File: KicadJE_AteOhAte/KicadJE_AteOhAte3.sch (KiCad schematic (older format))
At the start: 60 parts, among them U301 TL072, U302 TL072

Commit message: RIAA Basic Circuit
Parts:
- removed C301, C302, C303, C304: 10n, Capacitor_SMD:C_0805_2012Metric_Pad1.15x1.40mm_HandSolder, symbol Device:C
- removed D301, D302, D304, D305, D306, D307: LL4148, Diode_SMD:D_MiniMELF, symbol Diode:LL4148
- removed J? (x2): Conn_Coaxial_x2, symbol Connector:Conn_Coaxial_x2
- removed R301, R304, R306, R311, R316, R319, R322, R324: 1k, Resistor_SMD:R_0805_2012Metric_Pad1.15x1.40mm_HandSolder, symbol Device:R
- removed R303, R308, R314, R317, R318, R327, R329: 10k, Resistor_SMD:R_0805_2012Metric_Pad1.15x1.40mm_HandSolder, symbol Device:R
- removed R309, R323: 10R, Resistor_SMD:R_0805_2012Metric_Pad1.15x1.40mm_HandSolder, symbol Device:R
- removed R313, R315: 100k, Resistor_SMD:R_0805_2012Metric_Pad1.15x1.40mm_HandSolder, symbol Device:R
- removed R320, R321: Open, Resistor_SMD:R_0805_2012Metric_Pad1.15x1.40mm_HandSolder, symbol Device:R
- removed R325, R326: 0R, Resistor_SMD:R_0805_2012Metric_Pad1.15x1.40mm_HandSolder, symbol Device:R
- removed R328, R330: OPEN, Resistor_SMD:R_0805_2012Metric_Pad1.15x1.40mm_HandSolder, symbol Device:R
- added C305, C306, C315, C316: 10u, Capacitor_THT:CP_Radial_D6.3mm_P2.50mm, symbol Device:CP
- added C? (x4): 47p, symbol Device:C_Small
- added C? (x2): 100u, Capacitor_THT:CP_Radial_D6.3mm_P2.50mm, symbol Device:CP
- added C? (x4): 470n, symbol Device:C_Small
- added C? (x6): 470n_THT, Capacitor_THT:C_Rect_L7.2mm_W5.5mm_P5.00mm_FKS2_FKP2_MKS2_MKP2, symbol Device:C_Small
- added C? (x2): 470n, Capacitor_SMD:C_1206_3216Metric_Pad1.42x1.75mm_HandSolder, symbol Device:C_Small
- added C? (x2): 1n_THT, Capacitor_THT:C_Rect_L7.2mm_W5.5mm_P5.00mm_FKS2_FKP2_MKS2_MKP2, symbol Device:C_Small
- added C? (x2): 1n, Capacitor_SMD:C_1206_3216Metric_Pad1.42x1.75mm_HandSolder, symbol Device:C_Small
- added C? (x2): 680p_THT, Capacitor_THT:C_Rect_L7.2mm_W5.5mm_P5.00mm_FKS2_FKP2_MKS2_MKP2, symbol Device:C_Small
- added C? (x2): 680p, Capacitor_SMD:C_1206_3216Metric_Pad1.42x1.75mm_HandSolder, symbol Device:C_Small
- added C? (x2): 2n2_THT, Capacitor_THT:C_Rect_L7.2mm_W5.5mm_P5.00mm_FKS2_FKP2_MKS2_MKP2, symbol Device:C_Small
- added C? (x2): 2n2, Capacitor_SMD:C_1206_3216Metric_Pad1.42x1.75mm_HandSolder, symbol Device:C_Small
- added C? (x2): 100n, Capacitor_SMD:C_0805_2012Metric_Pad1.15x1.40mm_HandSolder, symbol Device:C
- added J301: PJRAS2X2S01AUX, PJRAS2X2S01AUX, symbol PJRAS2X2S01AUX:PJRAS2X2S01AUX
- added R? (x2): 680k, Resistor_SMD:R_0805_2012Metric_Pad1.15x1.40mm_HandSolder, symbol Device:R
- added R? (x5): 470R, Resistor_SMD:R_0805_2012Metric_Pad1.15x1.40mm_HandSolder, symbol Device:R
- added R? (x2): 47k, Resistor_SMD:R_0805_2012Metric_Pad1.15x1.40mm_HandSolder, symbol Device:R
- added R? (x5): 2k2, Resistor_SMD:R_0805_2012Metric_Pad1.15x1.40mm_HandSolder, symbol Device:R
- added R?: 220R, Resistor_SMD:R_0805_2012Metric_Pad1.15x1.40mm_HandSolder, symbol Device:R
- added R? (x4): 18k, Resistor_SMD:R_0805_2012Metric_Pad1.15x1.40mm_HandSolder, symbol Device:R
- added R? (x2): 1M, Resistor_SMD:R_0805_2012Metric_Pad1.15x1.40mm_HandSolder, symbol Device:R
- added R? (x2): 82k, Resistor_SMD:R_0805_2012Metric_Pad1.15x1.40mm_HandSolder, symbol Device:R
- added U? (x3): TL072, AJ-Dropbox-Kicad:AJ_SO-8_5.3x6.2mm_P1.27mm, symbol Amplifier_Operational:TL072
- C307: renamed from C306; value 1u -> 10u
- C313: renamed from C310; value 1u -> 10u
- R302: value 10k -> 220R
- R304: renamed from R305; value 1k -> 2k2
- R305: renamed from R307; value 10k -> 470R
- R311: renamed from R310; value 1k -> 12k
- R312: value 10k -> 18k
- gave numbers to parts that had none: 2
- renumbered C308 to C309, C309 to C310
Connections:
- net labels added: L_GainOut, L_Rumble_Out, R_GainOut, R_Rumble_Out
- net labels removed: Out1_Dist, Out1_Final, Out2_Dist, Out2_Final
- wire segments 145 -> 242
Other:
- moved on the sheet: C307, C308, C313, C314, D303, D308, D309, D310, R302, R304, R305, R311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

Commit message: SCH Annotate
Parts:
- gave numbers to parts that had none: 57
- renumbered C305 to C331, C306 to C332, C307 to C333, C308 to C334, C309 to C336, C310 to C337, C311 to C339, C312 to C340, C313 to C341, C314 to C342, C315 to C343, C316 to C344, D308 to D301, D309 to D302, D310 to D303, D303 to D304, R302 to R301, R304 to R302, R305 to R307, R311 to R327, U301 to U302, U302 to U303

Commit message: RIAA RCA
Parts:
- J301: footprint PJRAS2X2S01AUX -> AJ:PJRAS2X2S01AUX_RCA
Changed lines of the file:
@@
 F 0 "J301" H 6475 6850 50  0001 L BNN
 F 1 "PJRAS2X2S01AUX" H 6475 6850 50  0001 L BNN
-F 2 "PJRAS2X2S01AUX" H 6475 6850 50  0001 L BNN
+F 2 "AJ:PJRAS2X2S01AUX_RCA" H 6475 6850 50  0001 L BNN
 F 3 "" H 6475 6850 50  0001 L BNN
 F 4 "PJRAS2X2S01AUX" H 6475 6850 50  0001 L BNN "Field4"
@@
 F 0 "J301" H 4425 6850 50  0001 L BNN
 F 1 "PJRAS2X2S01AUX" H 4425 6850 50  0001 L BNN
-F 2 "PJRAS2X2S01AUX" H 4425 6850 50  0001 L BNN
+F 2 "AJ:PJRAS2X2S01AUX_RCA" H 4425 6850 50  0001 L BNN
 F 3 "" H 4425 6850 50  0001 L BNN
 F 4 "PJRAS2X2S01AUX" H 4425 6850 50  0001 L BNN "Field4"

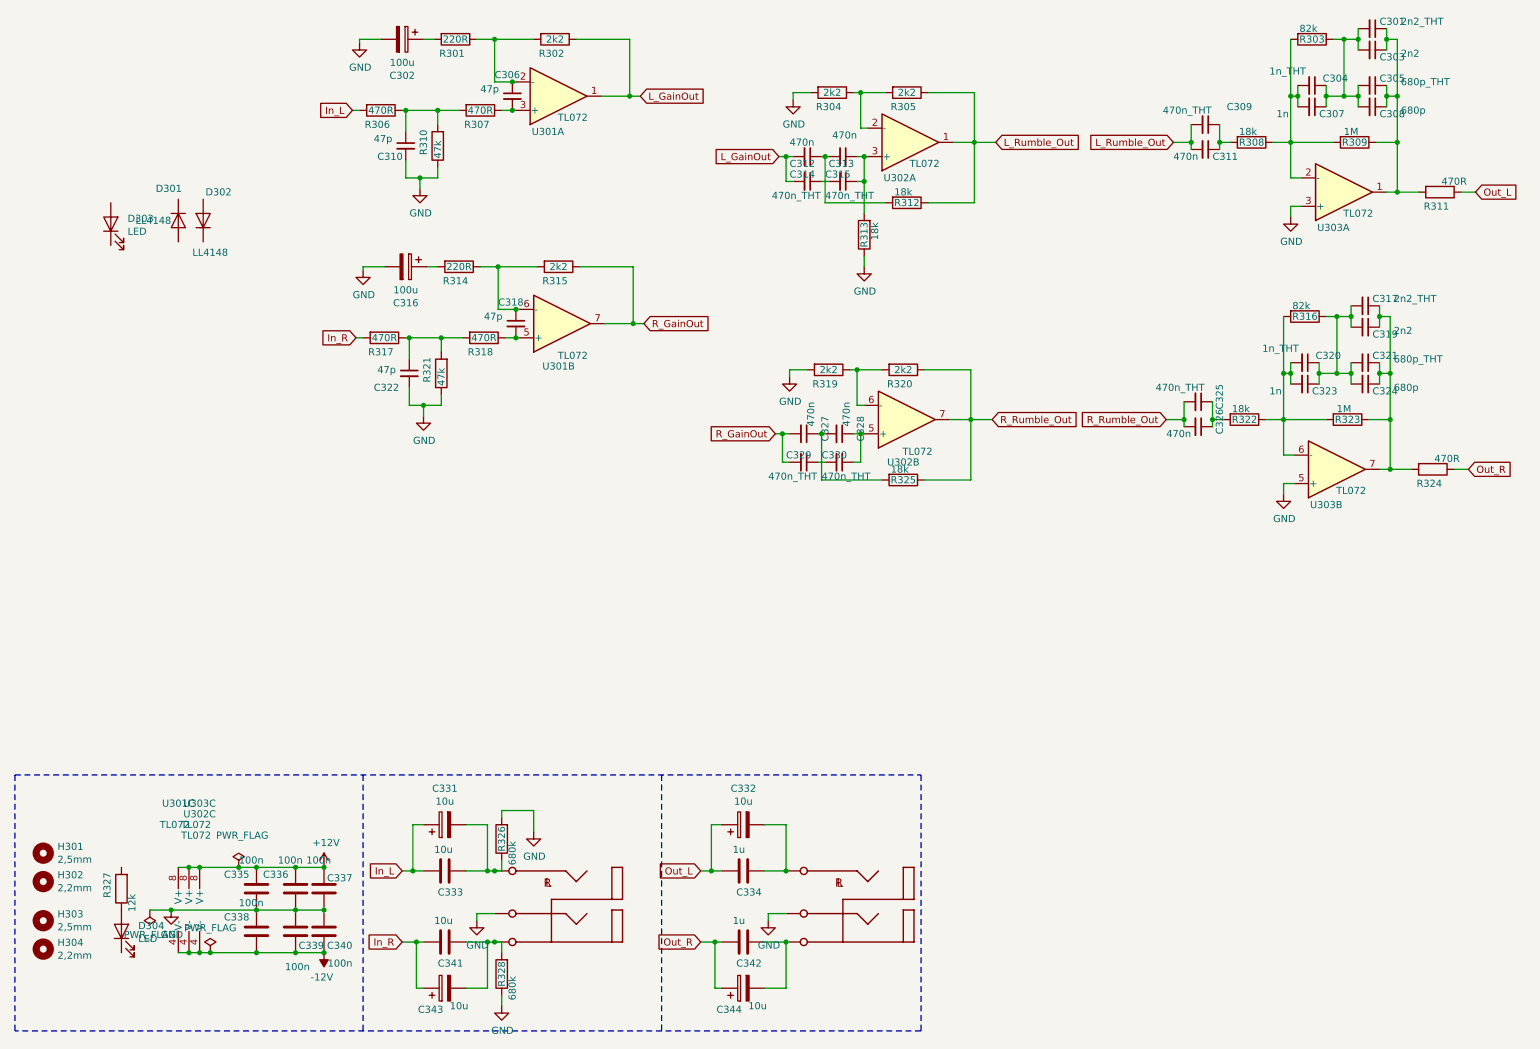
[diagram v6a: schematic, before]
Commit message: Capacirtor footprints
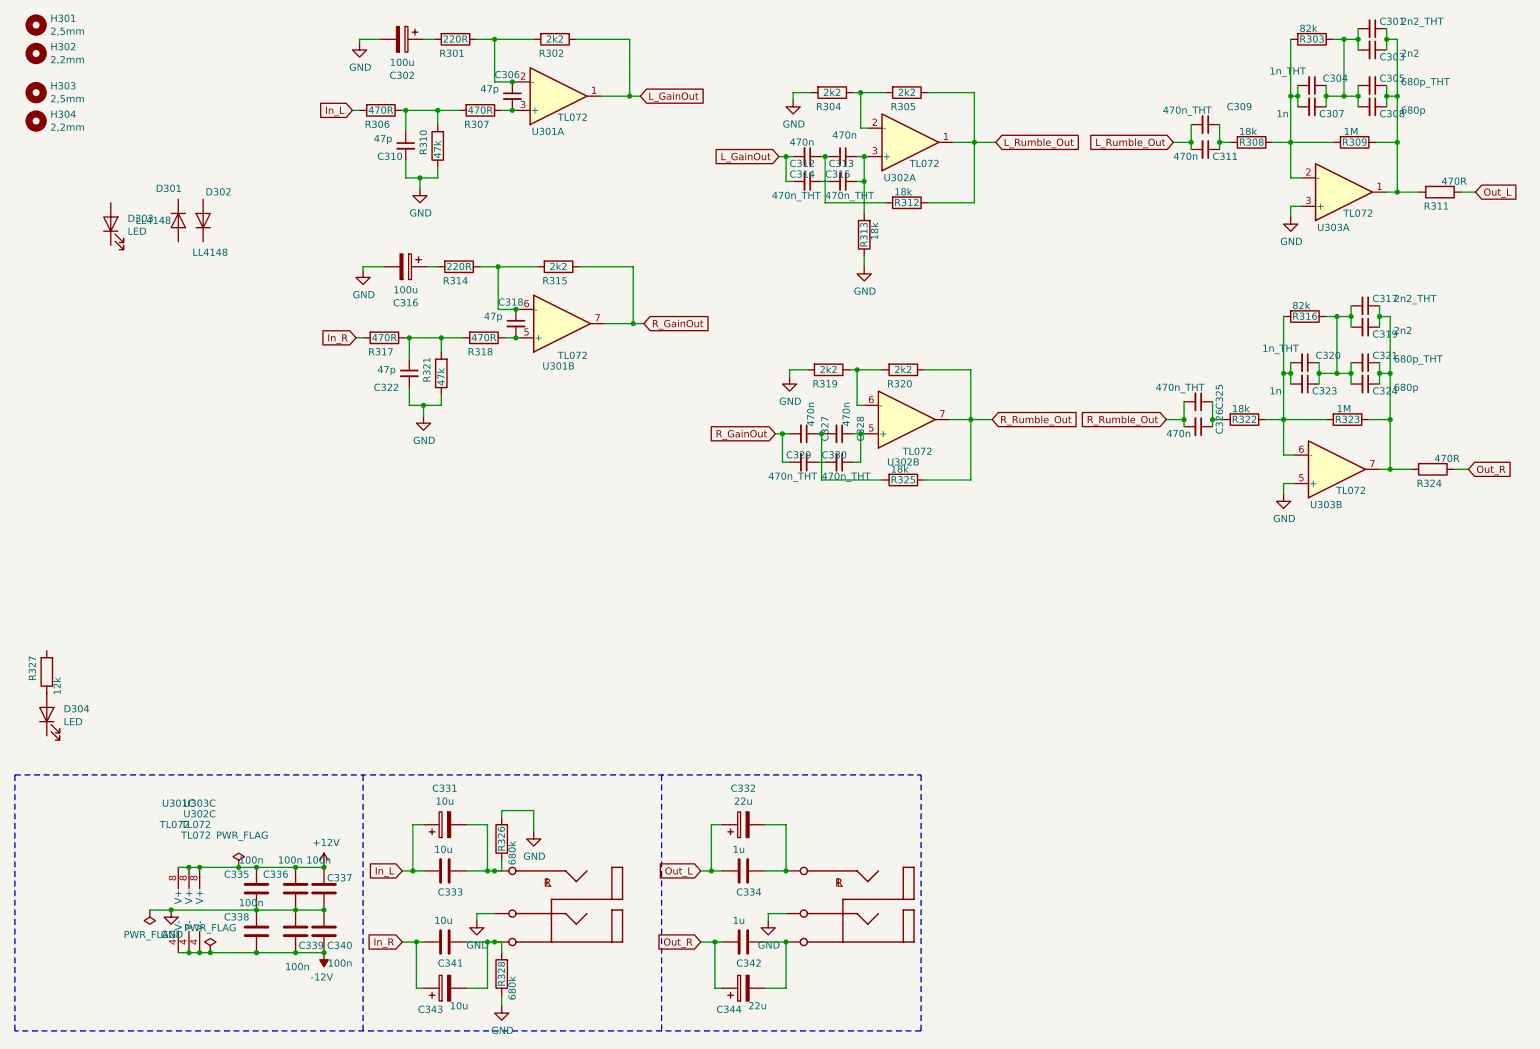
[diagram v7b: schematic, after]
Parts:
- C302, C316: footprint Capacitor_THT:CP_Radial_D6.3mm_P2.50mm -> Capacitor_SMD:CP_Elec_8x6.5
- C303, C307, C308, C319, C323, C324: footprint Capacitor_SMD:C_1206_3216Metric_Pad1.42x1.75mm_HandSolder -> Capacitor_SMD:C_0805_2012Metric_Pad1.15x1.40mm_HandSolder
- C306, C310, C312, C313, C318, C322, C327, C328: footprint (none) -> Capacitor_SMD:C_0805_2012Metric_Pad1.15x1.40mm_HandSolder
- C331, C343: footprint Capacitor_THT:CP_Radial_D6.3mm_P2.50mm -> Capacitor_THT:CP_Radial_D8.0mm_P3.50mm
- C332, C344: value 10u -> 22u; footprint Capacitor_THT:CP_Radial_D6.3mm_P2.50mm -> Capacitor_THT:CP_Radial_D8.0mm_P3.50mm
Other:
- moved on the sheet: D304, H301, H302, H303, H304, R327
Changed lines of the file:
@@
 L Mechanical:MountingHole H?
 U 1 1 5D513A45
-P 750 6475
+P 700 650
 AR Path="/5CF11B19/5D513A45" Ref="H?"  Part="1"
 AR Path="/5D4DB58B/5D513A45" Ref="H?"  Part="1"
 AR Path="/5D4DB615/5D513A45" Ref="H301"  Part="1"
-F 0 "H301" H 850 6521 50  0000 L CNN
-F 1 "2,5mm" H 850 6430 50  0000 L CNN
-F 2 "MountingHole:MountingHole_2.5mm_Pad_Via" H 750 6475 50  0001 C CNN
-F 3 "~" H 750 6475 50  0001 C CNN
-	1    750  6475
+F 0 "H301" H 800 696 50  0000 L CNN
+F 1 "2,5mm" H 800 605 50  0000 L CNN
+F 2 "MountingHole:MountingHole_2.5mm_Pad_Via" H 700 650 50  0001 C CNN
+F 3 "~" H 700 650 50  0001 C CNN
+	1    700  650
 	1    0    0    -1
 $EndComp
@@
 L Mechanical:MountingHole H?
 U 1 1 5D513A4B
-P 750 6950
+P 700 1125
 AR Path="/5CF11B19/5D513A4B" Ref="H?"  Part="1"
 AR Path="/5D4DB58B/5D513A4B" Ref="H?"  Part="1"
 AR Path="/5D4DB615/5D513A4B" Ref="H303"  Part="1"
-F 0 "H303" H 850 6996 50  0000 L CNN
-F 1 "2,5mm" H 850 6905 50  0000 L CNN
-F 2 "MountingHole:MountingHole_2.5mm_Pad_Via" H 750 6950 50  0001 C CNN
-F 3 "~" H 750 6950 50  0001 C CNN
-	1    750  6950
+F 0 "H303" H 800 1171 50  0000 L CNN
+F 1 "2,5mm" H 800 1080 50  0000 L CNN
+F 2 "MountingHole:MountingHole_2.5mm_Pad_Via" H 700 1125 50  0001 C CNN
+F 3 "~" H 700 1125 50  0001 C CNN
+	1    700  1125
 	1    0    0    -1
 $EndComp
@@
 L Mechanical:MountingHole H?
 U 1 1 5D513A51
-P 750 7150
+P 700 1325
 AR Path="/5CF11B19/5D513A51" Ref="H?"  Part="1"
 AR Path="/5D4DB58B/5D513A51" Ref="H?"  Part="1"
 AR Path="/5D4DB615/5D513A51" Ref="H304"  Part="1"
-F 0 "H304" H 850 7196 50  0000 L CNN
-F 1 "2,2mm" H 850 7105 50  0000 L CNN
-F 2 "MountingHole:MountingHole_2.2mm_M2_Pad_Via" H 750 7150 50  0001 C CNN
-F 3 "~" H 750 7150 50  0001 C CNN
-	1    750  7150
+F 0 "H304" H 800 1371 50  0000 L CNN
+F 1 "2,2mm" H 800 1280 50  0000 L CNN
+F 2 "MountingHole:MountingHole_2.2mm_M2_Pad_Via" H 700 1325 50  0001 C CNN
+F 3 "~" H 700 1325 50  0001 C CNN
+	1    700  1325
 	1    0    0    -1
 $EndComp
@@
 L Mechanical:MountingHole H?
 U 1 1 5D513A57
-P 750 6675
+P 700 850
 AR Path="/5CF11B19/5D513A57" Ref="H?"  Part="1"
 AR Path="/5D4DB58B/5D513A57" Ref="H?"  Part="1"
 AR Path="/5D4DB615/5D513A57" Ref="H302"  Part="1"
-F 0 "H302" H 850 6721 50  0000 L CNN
-F 1 "2,2mm" H 850 6630 50  0000 L CNN
-F 2 "MountingHole:MountingHole_2.2mm_M2_Pad_Via" H 750 6675 50  0001 C CNN
-F 3 "~" H 750 6675 50  0001 C CNN
-	1    750  6675
+F 0 "H302" H 800 896 50  0000 L CNN
+F 1 "2,2mm" H 800 805 50  0000 L CNN
+F 2 "MountingHole:MountingHole_2.2mm_M2_Pad_Via" H 700 850 50  0001 C CNN
+F 3 "~" H 700 850 50  0001 C CNN
+	1    700  850
 	1    0    0    -1
 $EndComp
@@
 L Device:LED D304
 U 1 1 5DA59B0A
-P 1300 7025
-F 0 "D304" V 1339 6907 50  0000 R CNN
-F 1 "LED" V 1248 6907 50  0000 R CNN
-F 2 "LED_THT:LED_D3.0mm" H 1300 7025 50  0001 C CNN
-F 3 "~" H 1300 7025 50  0001 C CNN
-	1    1300 7025
+P 775 5500
+F 0 "D304" V 814 5382 50  0000 R CNN
+F 1 "LED" V 723 5382 50  0000 R CNN
+F 2 "LED_THT:LED_D3.0mm" H 775 5500 50  0001 C CNN
+F 3 "~" H 775 5500 50  0001 C CNN
+	1    775  5500
 	0    -1   -1   0
 $EndComp
@@
 L Device:R R?
 U 1 1 5DA66984
-P 1300 6725
+P 775 5200
 AR Path="/5CF11B19/5DA66984" Ref="R?"  Part="1"
 AR Path="/5D4DB615/5DA66984" Ref="R327"  Part="1"
-F 0 "R327" V 1400 6700 50  0000 C CNN
-F 1 "12k" V 1225 6825 50  0000 C CNN
-F 2 "Resistor_SMD:R_0805_2012Metric_Pad1.15x1.40mm_HandSolder" V 1230 6725 50  0001 C CNN
-F 3 "~" H 1300 6725 50  0001 C CNN
-	1    1300 6725
+F 0 "R327" V 875 5175 50  0000 C CNN
+F 1 "12k" V 700 5300 50  0000 C CNN
+F 2 "Resistor_SMD:R_0805_2012Metric_Pad1.15x1.40mm_HandSolder" V 705 5200 50  0001 C CNN
+F 3 "~" H 775 5200 50  0001 C CNN
+	1    775  5200
 	-1   0    0    1
 $EndComp
@@
 F 0 "C331" V 3830 6275 50  0000 C CNN
 F 1 "10u" V 3739 6275 50  0000 C CNN
-F 2 "Capacitor_THT:CP_Radial_D6.3mm_P2.50mm" H 3613 6125 50  0001 C CNN
+F 2 "Capacitor_THT:CP_Radial_D8.0mm_P3.50mm" H 3613 6125 50  0001 C CNN
 F 3 "~" H 3575 6275 50  0001 C CNN
 	1    3575 6275
@@
 F 0 "C343" V 3425 7525 50  0000 C CNN
 F 1 "10u" V 3450 7325 50  0000 C CNN
-F 2 "Capacitor_THT:CP_Radial_D6.3mm_P2.50mm" H 3613 7275 50  0001 C CNN
+F 2 "Capacitor_THT:CP_Radial_D8.0mm_P3.50mm" H 3613 7275 50  0001 C CNN
 F 3 "~" H 3575 7425 50  0001 C CNN
 	1    3575 7425
@@
 P 5675 7425
 F 0 "C344" V 5525 7525 50  0000 C CNN
-F 1 "10u" V 5550 7325 50  0000 C CNN
-F 2 "Capacitor_THT:CP_Radial_D6.3mm_P2.50mm" H 5713 7275 50  0001 C CNN
+F 1 "22u" V 5550 7325 50  0000 C CNN
+F 2 "Capacitor_THT:CP_Radial_D8.0mm_P3.50mm" H 5713 7275 50  0001 C CNN
 F 3 "~" H 5675 7425 50  0001 C CNN
 	1    5675 7425
@@
 P 5675 6275
 F 0 "C332" V 5930 6275 50  0000 C CNN
-F 1 "10u" V 5839 6275 50  0000 C CNN
-F 2 "Capacitor_THT:CP_Radial_D6.3mm_P2.50mm" H 5713 6125 50  0001 C CNN
+F 1 "22u" V 5839 6275 50  0000 C CNN
+F 2 "Capacitor_THT:CP_Radial_D8.0mm_P3.50mm" H 5713 6125 50  0001 C CNN
 F 3 "~" H 5675 6275 50  0001 C CNN
 	1    5675 6275
@@
 F 0 "C306" H 3925 1300 50  0000 L CNN
 F 1 "47p" H 3825 1200 50  0000 L CNN
-F 2 "" H 4050 1150 50  0001 C CNN
+F 2 "Capacitor_SMD:C_0805_2012Metric_Pad1.15x1.40mm_HandSolder" H 4050 1150 50  0001 C CNN
 F 3 "~" H 4050 1150 50  0001 C CNN
 	1    4050 1150
@@
 F 0 "C310" H 3100 1425 50  0000 L CNN
 F 1 "47p" H 3075 1550 50  0000 L CNN
-F 2 "" H 3300 1500 50  0001 C CNN
+F 2 "Capacitor_SMD:C_0805_2012Metric_Pad1.15x1.40mm_HandSolder" H 3300 1500 50  0001 C CNN
 F 3 "~" H 3300 1500 50  0001 C CNN
 	1    3300 1500
@@
 F 0 "C302" V 3530 750 50  0000 C CNN
 F 1 "100u" V 3439 750 50  0000 C CNN
-F 2 "Capacitor_THT:CP_Radial_D6.3mm_P2.50mm" H 3313 600 50  0001 C CNN
+F 2 "Capacitor_SMD:CP_Elec_8x6.5" H 3313 600 50  0001 C CNN
 F 3 "~" H 3275 750 50  0001 C CNN
 	1    3275 750
@@
 F 0 "C312" V 6175 1450 50  0000 L CNN
 F 1 "470n" V 6025 1450 50  0000 L CNN
-F 2 "" H 6125 1575 50  0001 C CNN
+F 2 "Capacitor_SMD:C_0805_2012Metric_Pad1.15x1.40mm_HandSolder" H 6125 1575 50  0001 C CNN
 F 3 "~" H 6125 1575 50  0001 C CNN
 	1    6125 1575
@@
 F 0 "C313" V 6425 1475 50  0000 L CNN
 F 1 "470n" V 6225 1500 50  0000 L CNN
-F 2 "" H 6375 1575 50  0001 C CNN
+F 2 "Capacitor_SMD:C_0805_2012Metric_Pad1.15x1.40mm_HandSolder" H 6375 1575 50  0001 C CNN
 F 3 "~" H 6375 1575 50  0001 C CNN
 	1    6375 1575
@@
 F 0 "C318" H 3950 2900 50  0000 L CNN
 F 1 "47p" H 3850 2800 50  0000 L CNN
-F 2 "" H 4075 2750 50  0001 C CNN
+F 2 "Capacitor_SMD:C_0805_2012Metric_Pad1.15x1.40mm_HandSolder" H 4075 2750 50  0001 C CNN
 F 3 "~" H 4075 2750 50  0001 C CNN
 	1    4075 2750
@@
 F 0 "C322" H 3075 3000 50  0000 L CNN
 F 1 "47p" H 3100 3125 50  0000 L CNN
-F 2 "" H 3325 3100 50  0001 C CNN
+F 2 "Capacitor_SMD:C_0805_2012Metric_Pad1.15x1.40mm_HandSolder" H 3325 3100 50  0001 C CNN
 F 3 "~" H 3325 3100 50  0001 C CNN
 	1    3325 3100
@@
 F 0 "C316" V 3555 2350 50  0000 C CNN
 F 1 "100u" V 3464 2350 50  0000 C CNN
-F 2 "Capacitor_THT:CP_Radial_D6.3mm_P2.50mm" H 3338 2200 50  0001 C CNN
+F 2 "Capacitor_SMD:CP_Elec_8x6.5" H 3338 2200 50  0001 C CNN
 F 3 "~" H 3300 2350 50  0001 C CNN
 	1    3300 2350
@@
 F 0 "C327" H 5975 3675 50  0000 L CNN
 F 1 "470n" H 5875 3575 50  0000 L CNN
-F 2 "" H 6100 3525 50  0001 C CNN
+F 2 "Capacitor_SMD:C_0805_2012Metric_Pad1.15x1.40mm_HandSolder" H 6100 3525 50  0001 C CNN
 F 3 "~" H 6100 3525 50  0001 C CNN
 	1    6100 3525
@@
 F 0 "C328" H 6225 3675 50  0000 L CNN
 F 1 "470n" H 6125 3575 50  0000 L CNN
-F 2 "" H 6350 3525 50  0001 C CNN
+F 2 "Capacitor_SMD:C_0805_2012Metric_Pad1.15x1.40mm_HandSolder" H 6350 3525 50  0001 C CNN
 F 3 "~" H 6350 3525 50  0001 C CNN
 	1    6350 3525
@@
 F 0 "C307" V 9725 1275 50  0000 L CNN
 F 1 "1n" V 9725 975 50  0000 L CNN
-F 2 "Capacitor_SMD:C_1206_3216Metric_Pad1.42x1.75mm_HandSolder" H 9675 1225 50  0001 C CNN
+F 2 "Capacitor_SMD:C_0805_2012Metric_Pad1.15x1.40mm_HandSolder" H 9675 1225 50  0001 C CNN
 F 3 "~" H 9675 1225 50  0001 C CNN
 	1    9675 1225
@@
 F 0 "C308" V 10150 1275 50  0000 L CNN
 F 1 "680p" V 10125 1425 50  0000 L CNN
-F 2 "Capacitor_SMD:C_1206_3216Metric_Pad1.42x1.75mm_HandSolder" H 10100 1225 50  0001 C CNN
+F 2 "Capacitor_SMD:C_0805_2012Metric_Pad1.15x1.40mm_HandSolder" H 10100 1225 50  0001 C CNN
 F 3 "~" H 10100 1225 50  0001 C CNN
 	1    10100 1225
@@
 F 0 "C303" V 10150 875 50  0000 L CNN
 F 1 "2n2" V 10125 1025 50  0000 L CNN
-F 2 "Capacitor_SMD:C_1206_3216Metric_Pad1.42x1.75mm_HandSolder" H 10100 825 50  0001 C CNN
+F 2 "Capacitor_SMD:C_0805_2012Metric_Pad1.15x1.40mm_HandSolder" H 10100 825 50  0001 C CNN
 F 3 "~" H 10100 825 50  0001 C CNN
 	1    10100 825
@@
 F 0 "C323" V 9675 3225 50  0000 L CNN
 F 1 "1n" V 9675 2925 50  0000 L CNN
-F 2 "Capacitor_SMD:C_1206_3216Metric_Pad1.42x1.75mm_HandSolder" H 9625 3175 50  0001 C CNN
+F 2 "Capacitor_SMD:C_0805_2012Metric_Pad1.15x1.40mm_HandSolder" H 9625 3175 50  0001 C CNN
 F 3 "~" H 9625 3175 50  0001 C CNN
 	1    9625 3175
@@
 F 0 "C324" V 10100 3225 50  0000 L CNN
 F 1 "680p" V 10075 3375 50  0000 L CNN
-F 2 "Capacitor_SMD:C_1206_3216Metric_Pad1.42x1.75mm_HandSolder" H 10050 3175 50  0001 C CNN
+F 2 "Capacitor_SMD:C_0805_2012Metric_Pad1.15x1.40mm_HandSolder" H 10050 3175 50  0001 C CNN
 F 3 "~" H 10050 3175 50  0001 C CNN
 	1    10050 3175
@@
 F 0 "C319" V 10100 2825 50  0000 L CNN
 F 1 "2n2" V 10075 2975 50  0000 L CNN
-F 2 "Capacitor_SMD:C_1206_3216Metric_Pad1.42x1.75mm_HandSolder" H 10050 2775 50  0001 C CNN
+F 2 "Capacitor_SMD:C_0805_2012Metric_Pad1.15x1.40mm_HandSolder" H 10050 2775 50  0001 C CNN
 F 3 "~" H 10050 2775 50  0001 C CNN
 	1    10050 2775
